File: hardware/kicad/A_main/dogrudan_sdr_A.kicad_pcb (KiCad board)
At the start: 6 copper layers, 235 x 225 mm, 297 parts, among them J1 XT60, J10 JTAG 2x3, J20 SMA A1, J21 SMA B1, J22 SMA A2, J23 SMA B2, J30 SMA TX1, J31 SMA TX2, J32 SMA TX3, J33 SMA TX4, J40 HR911130A, J41 HR911130A, J60 GPS modul, J61 SMA 10MHz ref, J62 DAC modul, J63 C kartina, J64 UART 3.3V, J65 C kartina #2, J66 D kartina, Q1 DMP3098L, SW1 PROG, T1 ADT1-1WT+, T10 ADT1-1WT+, T11 ADT1-1WT+, T12 ADT1-1WT+, T13 ADT1-1WT+, T2 ADT1-1WT+, T3 ADT1-1WT+, T4 ADT1-1WT+, U1 TPS62130, U10 LFE5U-25F-7BG256I, U11 W25Q128JVSIQ, U15 ADCLK846BCPZ, U16 SN65LVDS2DBVR, U17 SN65LVDS2DBVR, U18 SN65LVDS2DBVR, U2 TPS62130, U20 AD9251BCPZ-80, U21 AD9251BCPZ-80, U3 TPS7A2033, U30 AD9767ASTZ, U31 AD9767ASTZ, U4 ADP150, U40 RTL8211FI-CG, U41 RTL8211FI-CG, U5 ADP150, U50 W9825G6KH-6I, U6 ADP150, U62 TLV3501AIDBVR, U7 ADP150, U8 ADP150, U9 ADP150, Y10 ABLNO-V-80.000MHZ, Y610 25MHz CL12pF, Y626 25MHz CL12pF

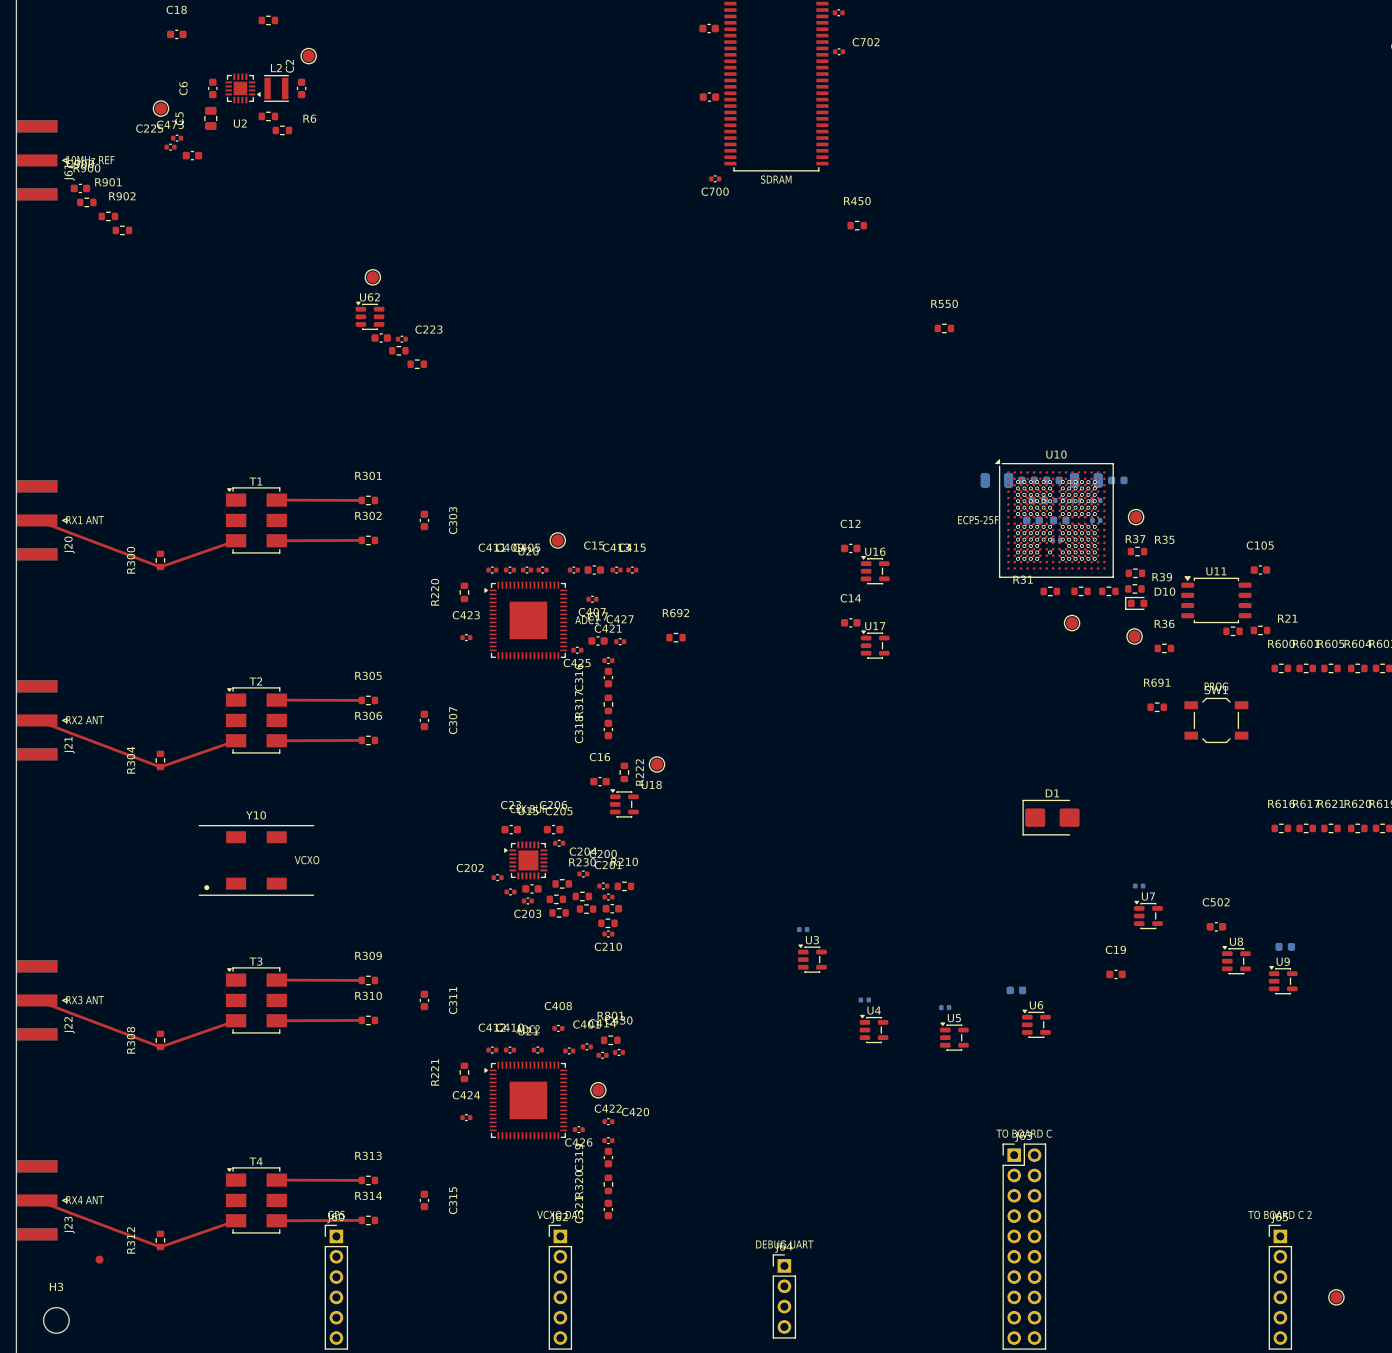
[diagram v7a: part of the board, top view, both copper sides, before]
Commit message: Compare symbol pins against footprint pads before placement
Every fault that would have stopped a board in this work sits in one
layer: a symbol pin number that does not agree with a footprint pad
number. The ADC paddle was pin 0 against pad 65. The attenuator
paddle was named Pad against pad 21. The gas discharge tubes used
pins 1 and 3 against pads 1 and 2. The crystal had two pins on a
four-pad part, so XO went to the can. The Ethernet PHY carried the
footprint of a different package. Each was found separately, by hand,
after it had already cost placement and routing time.

temel_denetim checks the whole class at once. For each part it
reports pins with no pad, where the net goes nowhere while the
schematic looks correct; pads with no pin, where copper is left
unconnected; and a count mismatch, which is the quickest sign that a
footprint belongs to another part.

It reads the symbols embedded in the schematics and not the library
file, because the library was edited by hand while its generator
stayed behind.

yap.sh runs it after pcb_kur and before placement, and stops there. A
wrong schematic makes everything below it worthless.

All three boards report zero. The parts it cannot check are those
with no symbol: mounting holes, fiducials and test points.
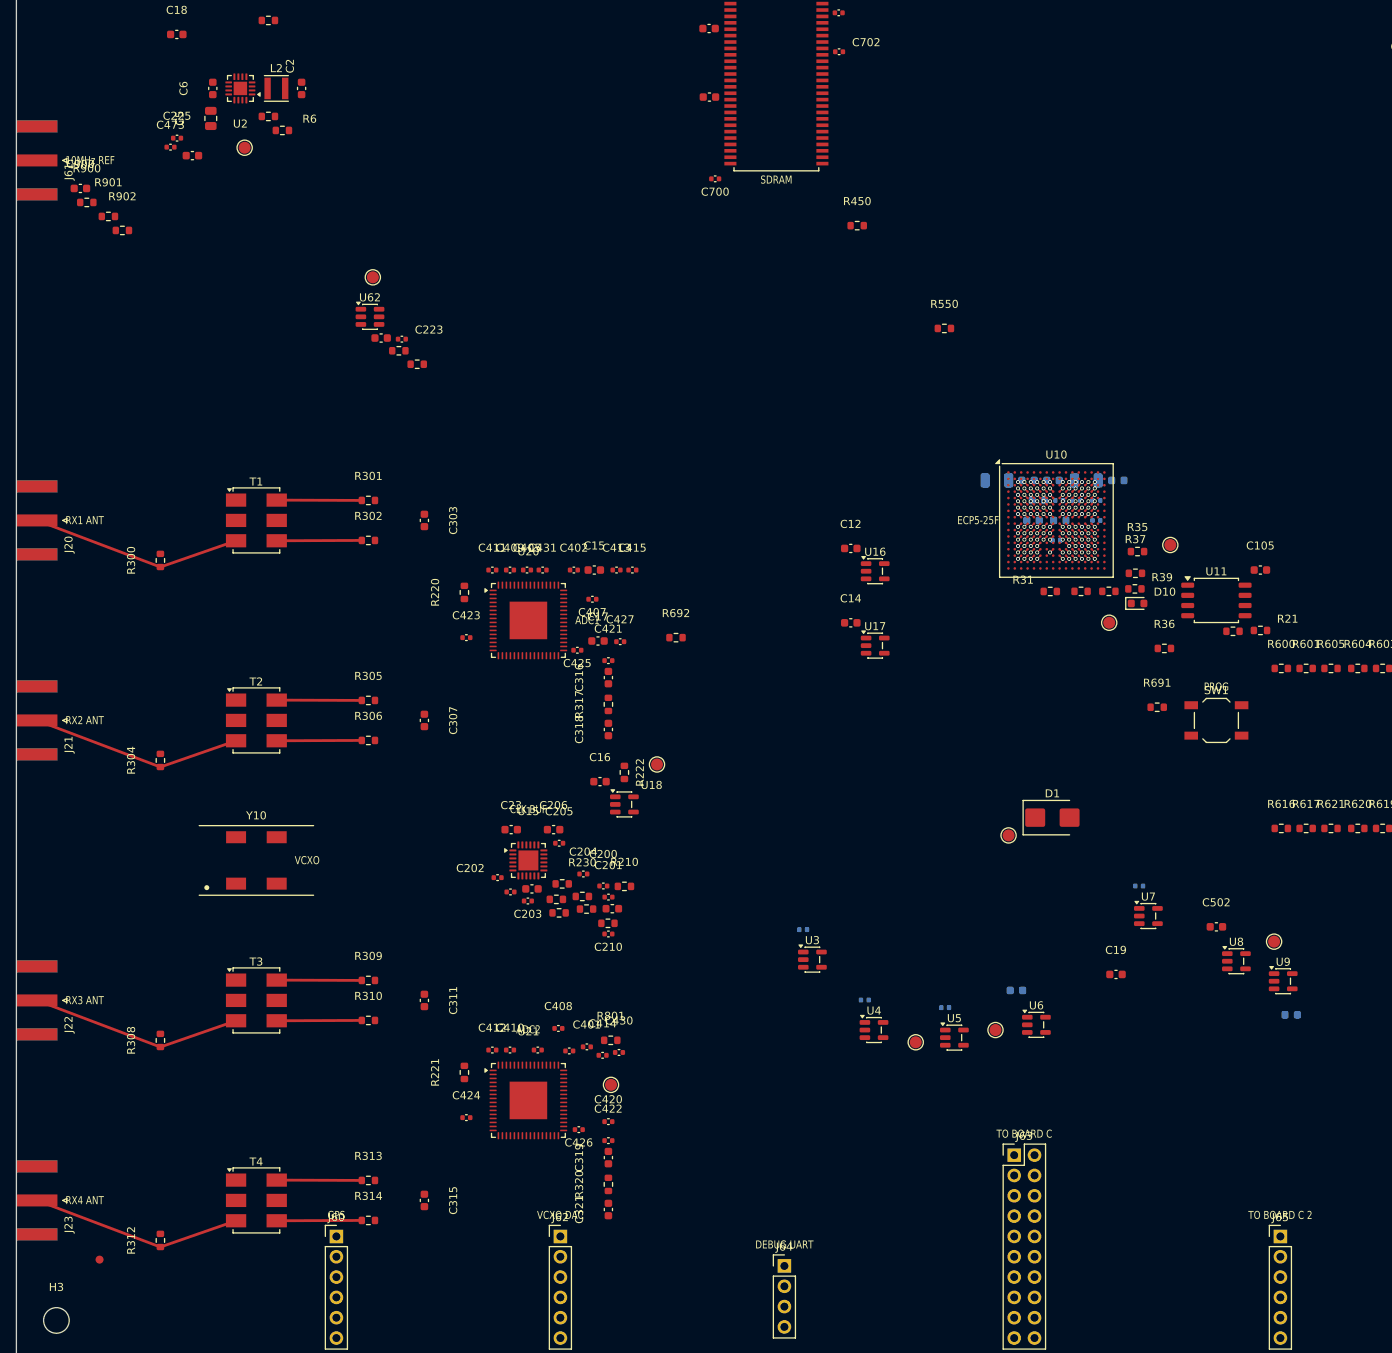
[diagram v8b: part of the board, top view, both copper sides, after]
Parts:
- moved TP5 150.1 mm to (112.4, 185.2)
- moved TP6 70.8 mm to (124.0, 159.4)
- moved TP2 68.4 mm to (74.3, 190.6)
- moved TP4 55.8 mm to (157.2, 172.7)
- moved TP3 50.2 mm to (122.4, 183.7)
- moved TP9 15.7 mm to (144.2, 123.1)
- moved TP1 14.0 mm to (28.5, 73.4)
- moved C13 8.53 mm to (159.3, 181.8)
- moved TP8 3.61 mm to (136.6, 132.8)
